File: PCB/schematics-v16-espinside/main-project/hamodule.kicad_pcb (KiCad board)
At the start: 2 copper layers, 76.7 x 84.3 mm, 83 parts, among them J1 2604-1104, J10 USB_B_Micro, J2 2604-1102, J4 ESP Relays, J5 Current Jumper, J6 GND 3.3V, J7 Conn_01x02, J8 Current Jumper, J9 2604-1104, K1 PCN-105D, K2 PCN-105D, K3 PCN-105D, K4 PCN-105D, Q1 2N2219, Q2 2N2219, SW1 EN-Switch, SW2 IO0-Switch, U1 ULN2003A, U2 ESP32-WROOM-32D, U3 CP2102N-A01-GQFN24, U4 LD1117AV33_TO220, U6 LDA210-PDIP, U7 LDA210-PDIP

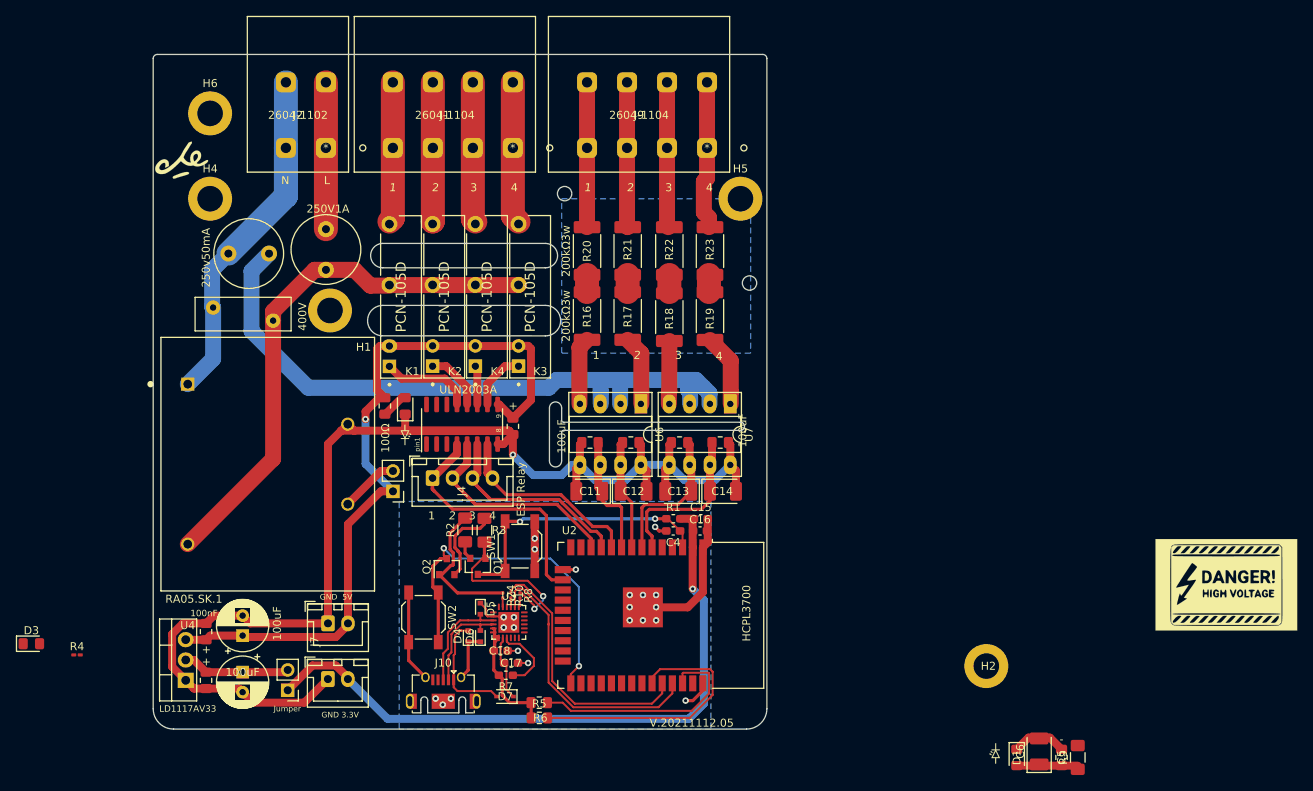
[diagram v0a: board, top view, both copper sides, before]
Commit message: fixing rules, missed connections, GND plane
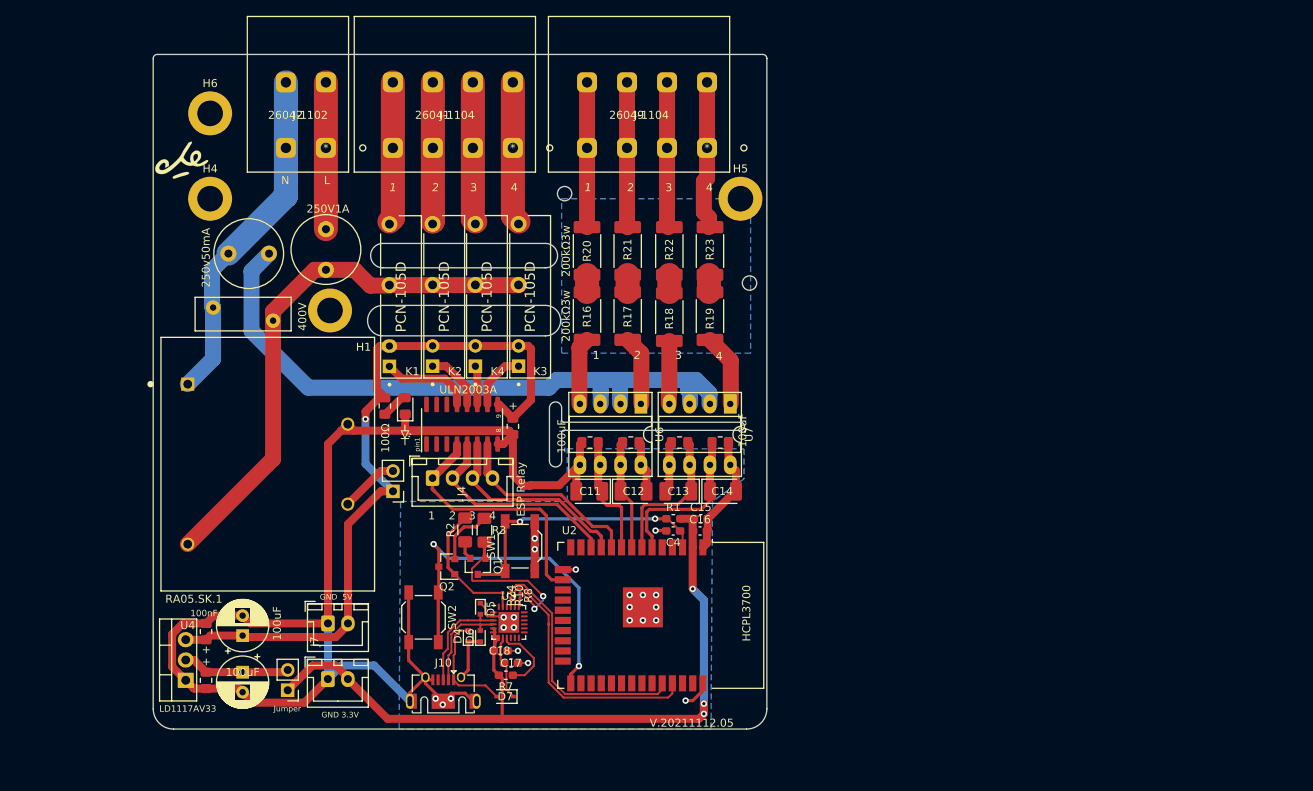
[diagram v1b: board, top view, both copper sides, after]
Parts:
- removed C5: 100nF, Capacitor_SMD:C_0805_2012Metric_Pad1.15x1.40mm_HandSolder
- removed C6: 22uF, Capacitor_Tantalum_SMD:CP_EIA-3528-21_Kemet-B_Pad1.50x2.35mm_HandSolder
- removed D1, D3: LED, LED_SMD:LED_0805_2012Metric_Pad1.15x1.40mm_HandSolder
- removed the G*** at (230.3, 154.7)
- removed H2: MountingHole_Pad, MountingHole:MountingHole_3.2mm_M3_ISO14580_Pad
- removed R4: 1kΩ, Resistor_SMD:R_0201_0603Metric_Pad0.64x0.40mm_HandSolder
- removed R5, R6: 4.7kΩ, Resistor_SMD:R_0805_2012Metric_Pad1.15x1.40mm_HandSolder
- removed R9: 100Ω, Resistor_SMD:R_1206_3216Metric_Pad1.42x1.75mm_HandSolder
- G***: moved to B.Cu
- moved G*** 99.0 mm to (164.3, 105.7)
- turned Q2 to 180 degrees
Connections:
- C15 pad 2: GND -> GND(5V)
- C16 pad 2: GND -> GND(5V)
- C17 pad 2: GND -> GND(5V)
- C18 pad 1: VDD3V3 -> 3.3V+
- C18 pad 2: GND -> GND(5V)
- C4 pad 2: GND -> GND(5V)
- D4 pad 1: GND -> GND(5V)
- D5 pad 1: GND -> GND(5V)
- D6 pad 1: GND -> GND(5V)
- J10 pad 5: GND -> GND(5V)
- J10 pad 6: GND -> GND(5V)
- R7 pad 2: VDD3V3 -> 3.3V+
- SW1 pad 2: GND -> GND(5V)
- SW2 pad 2: GND -> GND(5V)
- U1 pad 8: (no net) -> GND(5V)
- U2 pad 1: GND -> GND(5V)
- U2 pad 15: GND -> GND(5V)
- U2 pad 33: SDA -> (no net)
- U2 pad 36: SCL -> (no net)
- U2 pad 38: GND -> GND(5V)
- U2 pad 39: GND -> GND(5V)
- U3 pad 2: GND -> GND(5V)
- U3 pad 25: GND -> GND(5V)
- U3 pad 5: VDD3V3 -> 3.3V+
- U3 pad 6: VDD3V3 -> 3.3V+
- U3 pad 7: VDD3V3 -> 3.3V+
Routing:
- net GND(5V): track 174.3 -> 235.7 mm, vias 1 -> 22
- net GND: track 56.8 -> 0.00 mm, vias 22 -> 0
- net SDA: track 33.6 -> 0.00 mm
- net SCL: track 28.7 -> 0.00 mm
- net 3.3V+: track 82.4 -> 99.6 mm, vias 1 -> 3
- net VDD3V3: track 16.8 -> 0.00 mm
- net Net-(C5-Pad1): track 7.62 -> 0.00 mm
- net Net-(C5-Pad2): track 6.79 -> 0.00 mm
- net Net-(Q2-Pad2): track 10.4 -> 7.49 mm
- net DTR: track 17.9 -> 15.2 mm
- net RXD0: track 32.4 -> 31.1 mm
- net TXD0: track 35.0 -> 34.0 mm
- net Net-(D4-Pad2): track 14.3 -> 13.8 mm
- added copper zone on B.Cu, net GND(5V)
- removed copper zone on B.Cu, net GND
